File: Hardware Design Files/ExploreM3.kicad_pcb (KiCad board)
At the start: 2 copper layers, 25.5 x 62.1 mm, 66 parts, among them P1 CONN_02X05, P5 CONN_01X20, P6 GPIO'S, P7 CONN_01X20, SW1 SW_PUSH, SW2 SW_PUSH, U1 LPC1769FBD100, U10 MountingHole, U11 MountingHole, U12 MountingHole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

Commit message: Added filled zones
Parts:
- moved U5 1.28 mm to (56.0, 39.8)
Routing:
- added copper zone on B.Cu, net (none)
- added copper zone on F.Cu, net (none)
- added copper zone on F.Cu, net +3V3
- added copper zone on B.Cu, net GND
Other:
- net class Default: clearance 0.15 -> 0.1246
- rule trace_clearance: 0.15 -> 0.1246

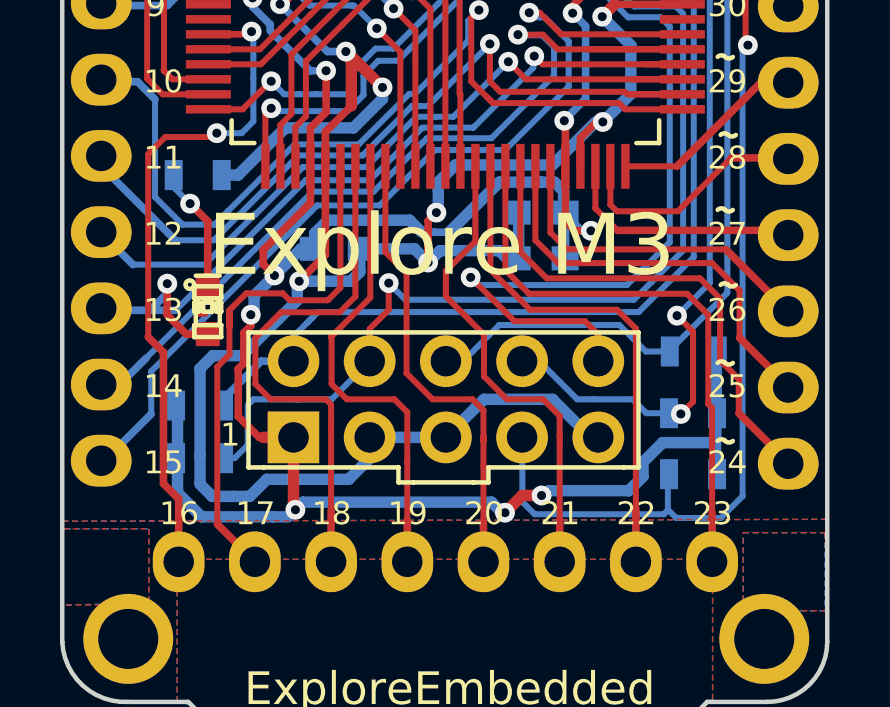
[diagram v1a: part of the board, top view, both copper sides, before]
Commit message: Moved LED
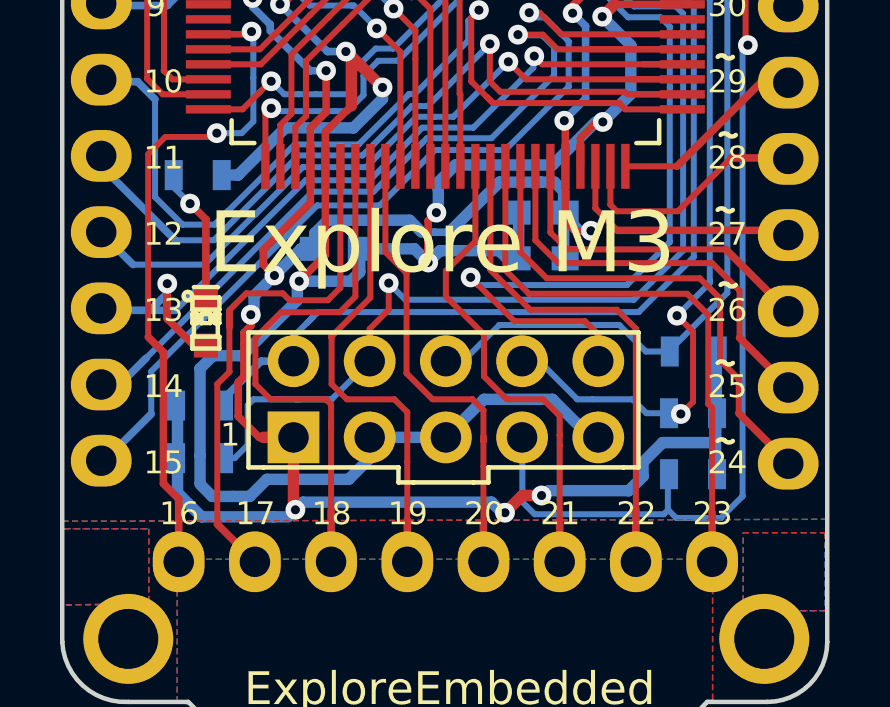
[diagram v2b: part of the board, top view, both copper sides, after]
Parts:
- moved D3 0.39 mm to (48.4, 76.1)
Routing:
- net /P0_6: track 29.8 -> 31.1 mm
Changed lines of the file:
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@@
     (links 165)
     (no_connects 0)
-    (area 39.841667 25.377 73.096429 90.319)
+    (area 39.867067 25.4024 73.071029 90.2936)
     (thickness 1.6)
     (drawings 74)
@@
   )
   (module EE:LED-0603_NEW (layer F.Cu)
-    (at 48.4505 75.692 90)
+    (at 48.387 76.073 90)
     (descr "LED 0603 smd package")
     (tags "LED led 0603 SMD smd SMT smt smdled SMDLED smtled SMTLED")
@@
     (effects (font (size 0.762 0.762) (thickness 0.1905)))
   )
-  (gr_text "Explore M3" (at 56.244328 73.488328) (layer F.SilkS)
+  (gr_text "Explore M3" (at 56.261 73.406) (layer F.SilkS)
     (effects (font (size 2.032 2.032) (thickness 0.508)))
   )
@@
     (effects (font (size 0.762 0.762) (thickness 0.1905)))
   )
-  (segment (start 48.103628 75.761628) (end 48.370328 75.761628) (width 0.2) (layer F.Cu) (net 0))
   (segment (start 58.59526 44.5008) (end 58.59526 43.87088) (width 0.2) (layer F.Cu) (net 1))
   (segment (start 58.59526 44.65574) (end 58.59526 44.5008) (width 0.2) (layer F.Cu) (net 1))
@@
   (segment (start 49.4665 79.1845) (end 50.165 79.883) (width 0.254) (layer F.Cu) (net 6))
   (segment (start 50.165 79.883) (end 51.308 79.883) (width 0.254) (layer F.Cu) (net 6))
-  (segment (start 49.657 76.7715) (end 49.657 77.4065) (width 0.254) (layer F.Cu) (net 6))
+  (segment (start 49.657 76.7715) (end 49.657 77.851) (width 0.254) (layer F.Cu) (net 6))
   (segment (start 49.8856 76.1619) (end 49.657 76.3905) (width 0.254) (layer F.Cu) (net 6))
   (segment (start 49.657 76.3905) (end 49.657 76.7715) (width 0.254) (layer F.Cu) (net 6))
@@
   (via (at 49.8856 75.7936) (size 0.66) (drill 0.3) (layers F.Cu B.Cu) (net 6))
   (segment (start 49.8856 75.7936) (end 49.8856 76.1619) (width 0.254) (layer F.Cu) (net 6))
-  (segment (start 49.657 77.4065) (end 49.4665 77.597) (width 0.254) (layer F.Cu) (net 6))
-  (segment (start 49.4665 77.597) (end 49.4665 79.1845) (width 0.254) (layer F.Cu) (net 6))
+  (segment (start 49.657 77.851) (end 49.4665 78.0415) (width 0.254) (layer F.Cu) (net 6))
+  (segment (start 49.4665 78.0415) (end 49.4665 79.1845) (width 0.254) (layer F.Cu) (net 6))
   (segment (start 57.871328 56.775128) (end 57.871328 57.576368) (width 0.2) (layer F.Cu) (net 7))
   (segment (start 57.871328 57.576368) (end 57.331448 58.116248) (width 0.2) (layer F.Cu) (net 7))
@@
   (segment (start 55.4355 69.723) (end 55.4355 69.725156) (width 0.2) (layer B.Cu) (net 31))
   (segment (start 57.303478 69.558978) (end 55.599522 69.558978) (width 0.2) (layer B.Cu) (net 31))
-  (segment (start 47.100328 75.802328) (end 47.7393 76.4413) (width 0.254) (layer F.Cu) (net 31))
-  (segment (start 47.7393 76.4413) (end 48.4505 76.4413) (width 0.254) (layer F.Cu) (net 31))
   (segment (start 44.941328 75.647329) (end 46.528828 75.647329) (width 0.2) (layer B.Cu) (net 31))
   (via (at 47.100328 74.758328) (size 0.66) (drill 0.3) (layers F.Cu B.Cu) (net 31))
@@
   (segment (start 46.528828 75.647329) (end 47.100329 75.075828) (width 0.254) (layer B.Cu) (net 31))
   (segment (start 47.100328 74.758328) (end 47.100328 75.802328) (width 0.254) (layer F.Cu) (net 31))
+  (segment (start 47.100328 75.929328) (end 47.100328 74.758328) (width 0.254) (layer F.Cu) (net 31))
+  (segment (start 47.9933 76.8223) (end 47.100328 75.929328) (width 0.254) (layer F.Cu) (net 31))
+  (segment (start 48.387 76.8223) (end 47.9933 76.8223) (width 0.254) (layer F.Cu) (net 31))
   (segment (start 44.941328 78.187328) (end 45.449328 78.187328) (width 0.254) (layer B.Cu) (net 32))
   (segment (start 45.449328 78.187328) (end 46.401828 77.234828) (width 0.254) (layer B.Cu) (net 32))
@@
   (segment (start 49.1744 75.6412) (end 49.1744 76.227556) (width 0.2) (layer F.Cu) (net 64))
   (segment (start 51.4604 75.311) (end 51.181 75.311) (width 0.2) (layer F.Cu) (net 64))
-  (segment (start 49.1744 77.1271) (end 48.768 77.5335) (width 0.2) (layer F.Cu) (net 64))
-  (segment (start 48.768 77.5335) (end 48.768 82.776001) (width 0.2) (layer F.Cu) (net 64))
+  (segment (start 49.1744 77.6986) (end 48.768 78.105) (width 0.2) (layer F.Cu) (net 64))
+  (segment (start 48.768 78.105) (end 48.768 82.776001) (width 0.2) (layer F.Cu) (net 64))
   (segment (start 48.768 82.776001) (end 50.021328 84.029329) (width 0.254) (layer F.Cu) (net 64))
-  (segment (start 49.1744 75.6412) (end 49.1744 77.1271) (width 0.2) (layer F.Cu) (net 64))
+  (segment (start 49.1744 75.6412) (end 49.1744 77.6986) (width 0.2) (layer F.Cu) (net 64))
   (segment (start 64.257328 32.530828) (end 64.257328 31.881672) (width 0.254) (layer B.Cu) (net 65))
   (segment (start 64.484472 31.654528) (end 63.546828 31.654528) (width 0.254) (layer F.Cu) (net 65))
@@
   (segment (start 47.862328 72.091328) (end 47.366328 71.595328) (width 0.2) (layer B.Cu) (net 66))
   (segment (start 47.366328 71.595328) (end 47.366328 71.138829) (width 0.2) (layer B.Cu) (net 66))
-  (segment (start 48.4505 72.6795) (end 47.862328 72.091328) (width 0.254) (layer F.Cu) (net 66))
-  (segment (start 48.4505 74.9427) (end 48.4505 72.6795) (width 0.254) (layer F.Cu) (net 66))
+  (segment (start 48.387 72.616) (end 47.862328 72.091328) (width 0.254) (layer F.Cu) (net 66))
+  (segment (start 48.387 75.3237) (end 48.387 72.616) (width 0.254) (layer F.Cu) (net 66))
   (segment (start 57.6 34.4) (end 57.6 36.6) (width 0.381) (layer F.Cu) (net 67))
   (segment (start 57.6 36.6) (end 59.227 38.227) (width 0.381) (layer F.Cu) (net 67))

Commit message: Version name modified on Silkscreen
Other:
- board text added: "v1.0"
- board text removed: "v0.3"
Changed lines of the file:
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@@
-(kicad_pcb (version 4) (host pcbnew "(2015-01-16 BZR 5376)-product")
+(kicad_pcb (version 4) (host pcbnew 4.0.1-stable)
   (general
     (links 165)
     (no_connects 0)
-    (area 39.867067 25.4024 73.071029 90.2936)
+    (area 43.524999 27.524999 69.175001 89.775001)
     (thickness 1.6)
     (drawings 74)
@@
   (page A4)
   (layers
-    (0 F.Cu signal)
-    (31 B.Cu signal)
+    (0 F.Cu signal hide)
+    (31 B.Cu signal hide)
     (32 B.Adhes user)
     (33 F.Adhes user)
@@
   (gr_arc (start 67.1 86.7) (end 69.1 86.7) (angle 90) (layer Edge.Cuts) (width 0.15))
   (gr_arc (start 45.7 86.6) (end 45.8 88.7) (angle 90) (layer Edge.Cuts) (width 0.15))
-  (gr_text v0.3 (at 56.4 36.7) (layer B.SilkS)
+  (gr_text v1.0 (at 56.4 36.7) (layer B.SilkS)
     (effects (font (size 0.762 0.762) (thickness 0.1905)) (justify mirror))
   )
